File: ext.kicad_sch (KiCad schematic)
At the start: 69 parts, among them J10 Conn_01x03, J11 Conn_01x03, J12 Conn_01x03, J2 Conn_01x06, J3 Conn_01x02, J4 Conn_01x03, J5 Conn_01x03, J6 Conn_01x03, J7 Conn_01x03, J9 Conn_01x03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

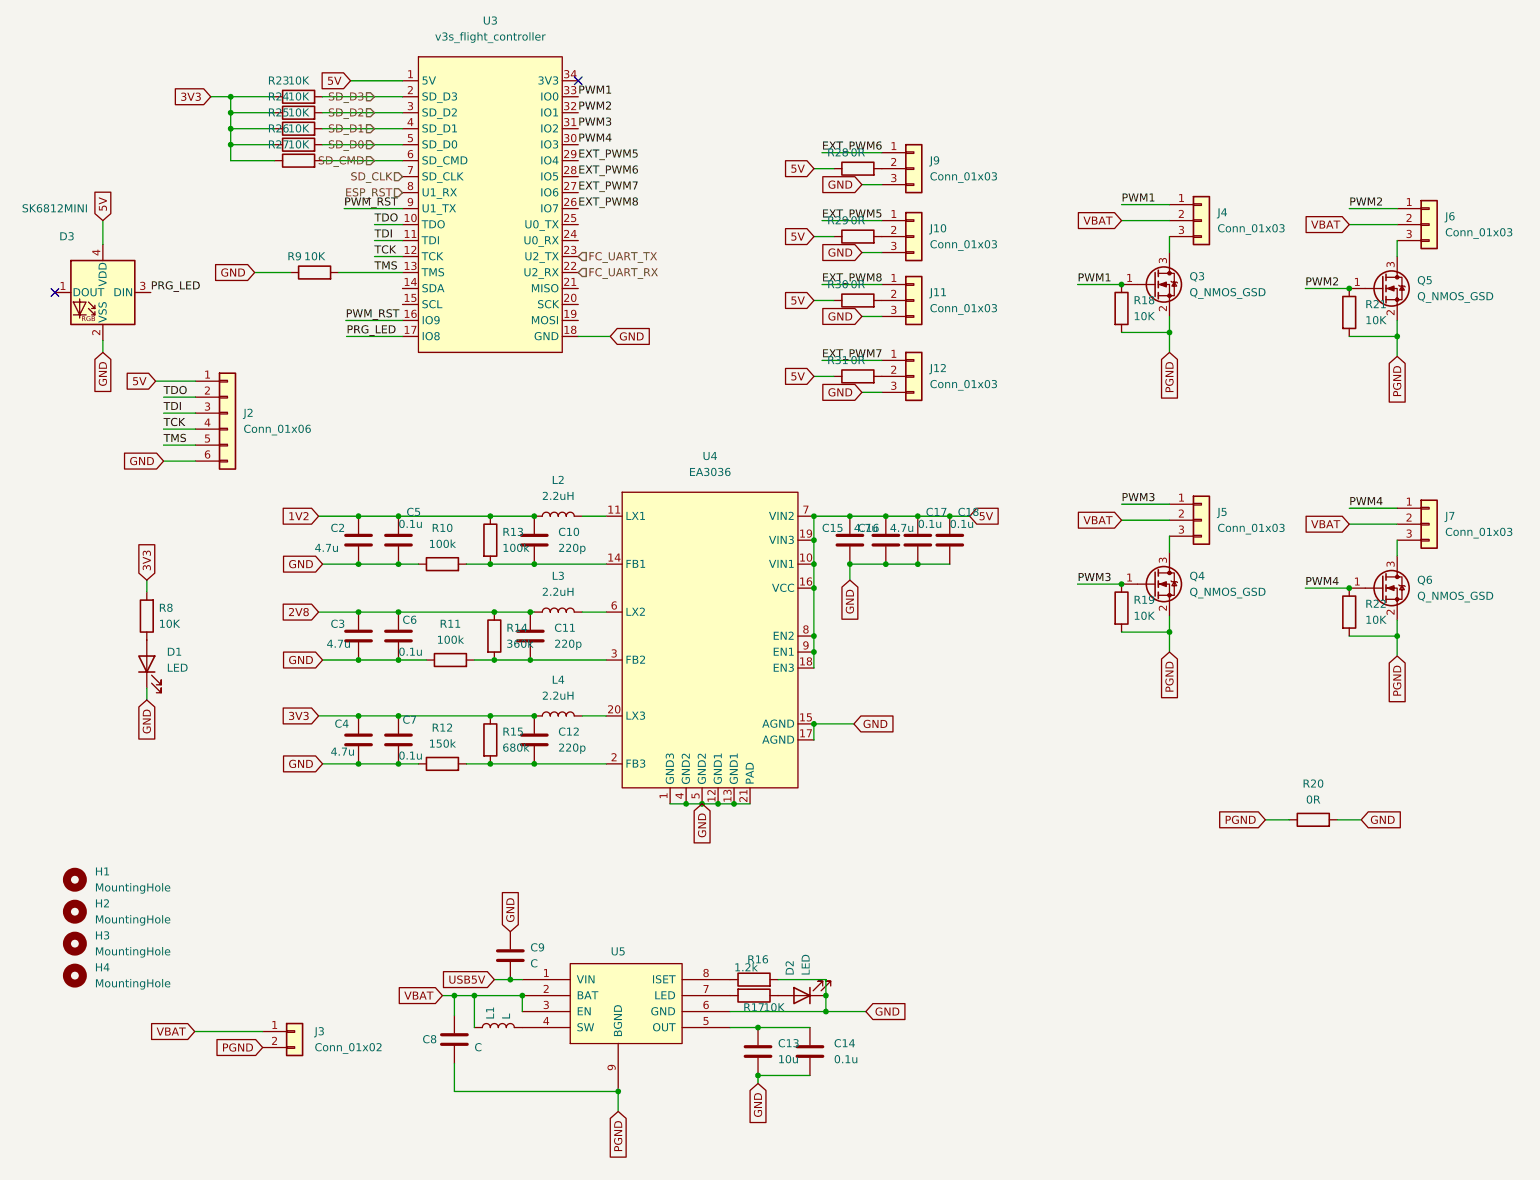
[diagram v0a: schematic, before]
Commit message: add images/docs/mechanical and Readme
Signed-off-by: ncerzzk <huangzzk@bupt.edu.cn>
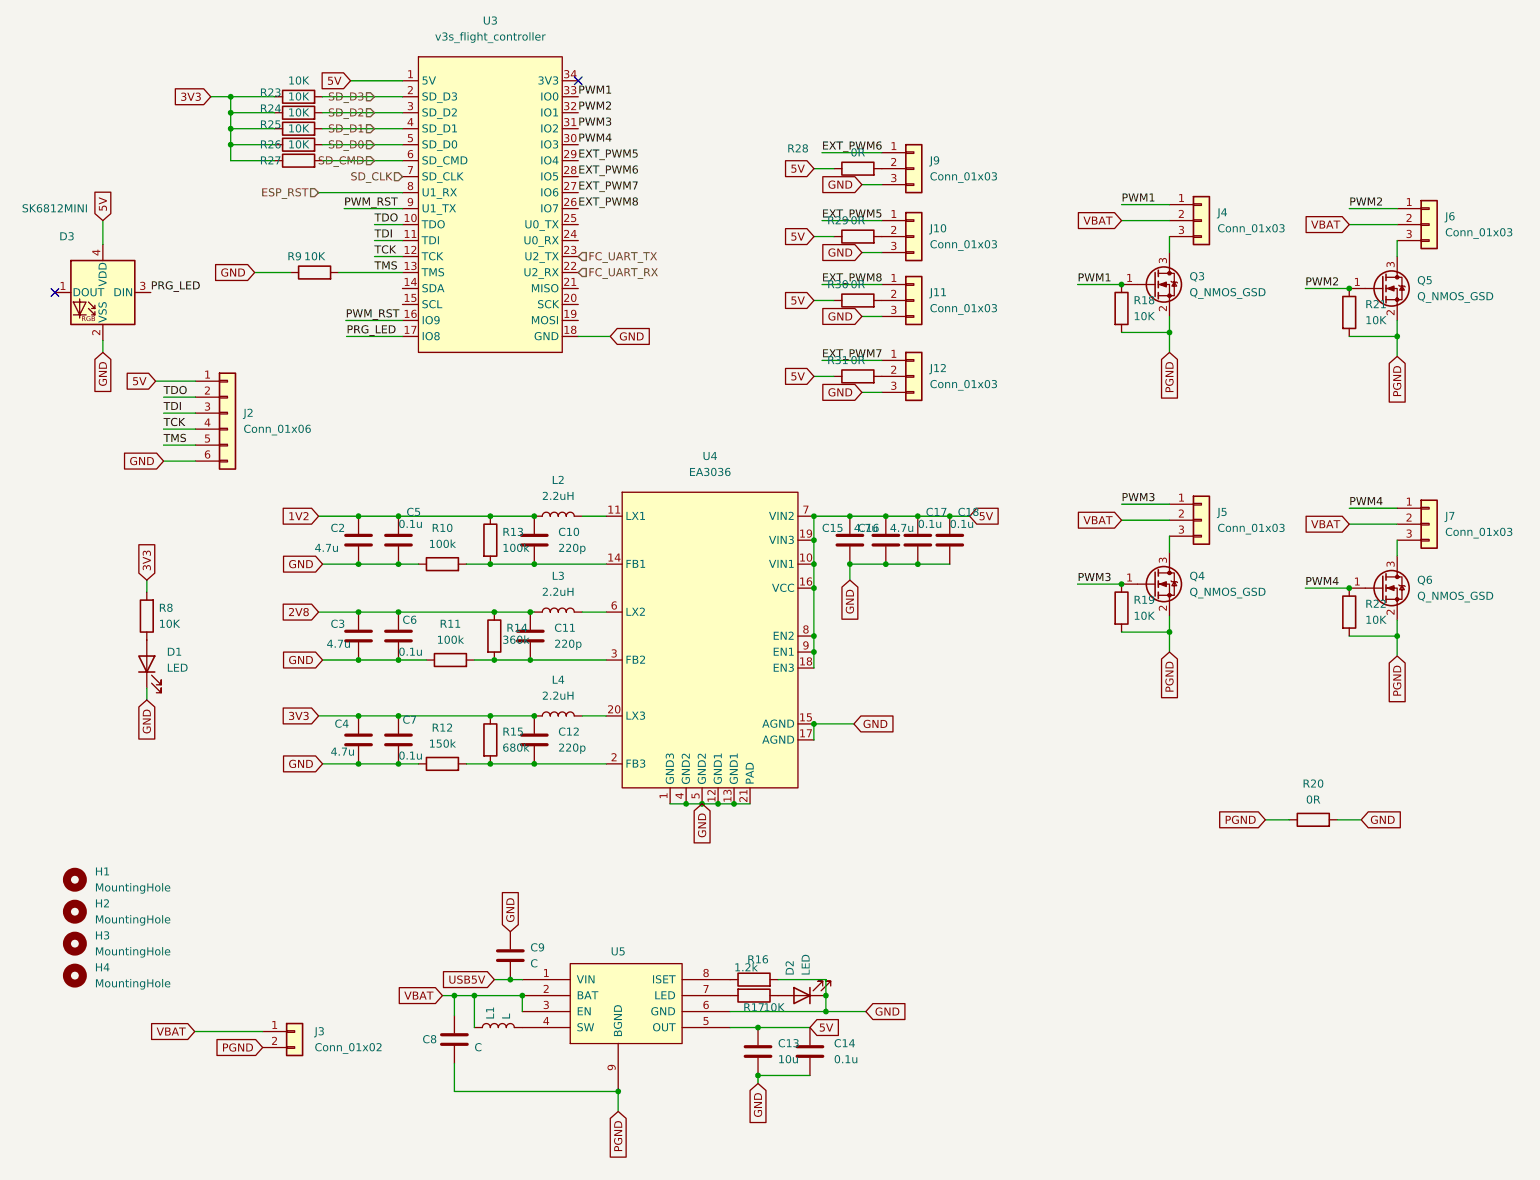
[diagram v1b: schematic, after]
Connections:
- net 5V: now also C13.1, C14.1, U5.5 (OUT)
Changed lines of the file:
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@@
+    (stroke (width 0) (type default) (color 0 0 0 0))
+  )
+  (wire (pts (xy 63.5 40.64) (xy 76.835 40.64))
     (stroke (width 0) (type default) (color 0 0 0 0))
   )
@@
     )
   )
+  (global_label "5V" (shape input) (at 141.605 173.355 0) (fields_autoplaced)
+    (effects (font (size 1.27 1.27)) (justify left))
+    (property "Intersheet References" "${INTERSHEET_REFS}" (id 0) (at 146.3162 173.2756 0)
+      (effects (font (size 1.27 1.27)) (justify left) hide)
+    )
+  )
   (global_label "PGND" (shape input) (at 213.995 140.335 180) (fields_autoplaced)
     (effects (font (size 1.27 1.27)) (justify right))
@@
     (effects (font (size 1.27 1.27)) (justify right))
   )
-  (hierarchical_label "ESP_RST" (shape input) (at 76.835 40.64 180)
+  (hierarchical_label "ESP_RST" (shape input) (at 63.5 40.64 180)
     (effects (font (size 1.27 1.27)) (justify right))
   )
@@
   )
   (symbol (lib_id "Device:R") (at 91.44 111.125 0) (unit 1)
-    (in_bom yes) (on_board yes) (fields_autoplaced)
+    (in_bom yes) (on_board yes)
     (property "Reference" "R14" (id 0) (at 93.345 109.8549 0)
       (effects (font (size 1.27 1.27)) (justify left))
     )
-    (property "Value" "360k" (id 1) (at 93.345 112.3949 0)
+    (property "Value" "360k" (id 1) (at 92.71 111.76 0)
       (effects (font (size 1.27 1.27)) (justify left))
     )
@@
   (symbol (lib_id "Device:R") (at 60.325 27.94 90) (unit 1)
     (in_bom yes) (on_board yes)
-    (property "Reference" "R24" (id 0) (at 57.15 25.4 90))
+    (property "Reference" "R24" (id 0) (at 55.88 27.305 90))
     (property "Value" "10K" (id 1) (at 60.325 25.4 90))
     (property "Footprint" "Resistor_SMD:R_0603_1608Metric" (id 2) (at 60.325 29.718 90)
@@
   (symbol (lib_id "Device:R") (at 149.225 36.83 90) (unit 1)
     (in_bom yes) (on_board yes)
-    (property "Reference" "R28" (id 0) (at 146.05 34.29 90))
+    (property "Reference" "R28" (id 0) (at 139.7 33.655 90))
     (property "Value" "0R" (id 1) (at 149.225 34.29 90))
     (property "Footprint" "Resistor_SMD:R_0603_1608Metric" (id 2) (at 149.225 38.608 90)
@@
   (symbol (lib_id "Device:R") (at 60.325 25.4 90) (unit 1)
     (in_bom yes) (on_board yes)
-    (property "Reference" "R23" (id 0) (at 57.15 22.86 90))
+    (property "Reference" "R23" (id 0) (at 55.88 24.765 90))
     (property "Value" "10K" (id 1) (at 60.325 22.86 90))
     (property "Footprint" "Resistor_SMD:R_0603_1608Metric" (id 2) (at 60.325 27.178 90)
@@
   (symbol (lib_id "Device:R") (at 60.325 30.48 90) (unit 1)
     (in_bom yes) (on_board yes)
-    (property "Reference" "R25" (id 0) (at 57.15 27.94 90))
+    (property "Reference" "R25" (id 0) (at 55.88 29.845 90))
     (property "Value" "10K" (id 1) (at 60.325 27.94 90))
     (property "Footprint" "Resistor_SMD:R_0603_1608Metric" (id 2) (at 60.325 32.258 90)
@@
   (symbol (lib_id "Device:R") (at 60.325 35.56 90) (unit 1)
     (in_bom yes) (on_board yes)
-    (property "Reference" "R27" (id 0) (at 57.15 33.02 90))
+    (property "Reference" "R27" (id 0) (at 55.88 35.56 90))
     (property "Value" "10K" (id 1) (at 60.325 33.02 90))
     (property "Footprint" "Resistor_SMD:R_0603_1608Metric" (id 2) (at 60.325 37.338 90)
@@
   (symbol (lib_id "Device:R") (at 60.325 33.02 90) (unit 1)
     (in_bom yes) (on_board yes)
-    (property "Reference" "R26" (id 0) (at 57.15 30.48 90))
+    (property "Reference" "R26" (id 0) (at 55.88 33.02 90))
     (property "Value" "10K" (id 1) (at 60.325 30.48 90))
     (property "Footprint" "Resistor_SMD:R_0603_1608Metric" (id 2) (at 60.325 34.798 90)
